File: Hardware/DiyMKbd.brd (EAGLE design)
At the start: 83 x 98 mm, 68 parts

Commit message: add gerber file
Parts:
- J1: value (none) -> 2.54 header
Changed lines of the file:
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@@
 <setting verticaltext="up"/>
 </settings>
-<grid distance="1" unitdist="mm" unit="mm" style="lines" multiple="1" display="yes" altdistance="0.025" altunitdist="inch" altunit="mm"/>
+<grid distance="0.5" unitdist="mm" unit="mm" style="lines" multiple="1" display="yes" altdistance="0.025" altunitdist="inch" altunit="mm"/>
 <layers>
 <layer number="1" name="Top" color="4" fill="1" visible="yes" active="yes"/>
@@
 <attribute name="VALUE" x="49.106" y="88.44" size="0.6096" layer="27" font="vector" ratio="20" rot="R270" align="top-center"/>
 </element>
-<element name="J1" library="SparkFun-Connectors" package="1X03_LOCK" value="" x="45.23" y="93.84" smashed="yes" rot="R270">
+<element name="J1" library="SparkFun-Connectors" package="1X03_LOCK" value="2.54 header" x="45.23" y="93.84" smashed="yes" rot="R270">
 <attribute name="NAME" x="47.627" y="95.11" size="1.016" layer="25" font="vector" rot="R270"/>
 <attribute name="VALUE" x="43.198" y="95.11" size="0.6096" layer="27" font="vector" ratio="20" rot="R270"/>
@@
 </element>
 <element name="D5" library="diode" package="SOD-123_MINI-SMA" value="CGRM4001-G" x="22.5" y="13" smashed="yes" rot="R270">
-<attribute name="NAME" x="23.643" y="16.048" size="1.016" layer="25" font="vector" rot="R270"/>
+<attribute name="NAME" x="22.143" y="10.048" size="1.016" layer="25" font="vector" rot="R270"/>
 <attribute name="VALUE" x="20.087" y="16.048" size="1.27" layer="27" rot="R270"/>
 </element>
 <element name="D1" library="diode" package="SOD-123_MINI-SMA" value="CGRM4001-G" x="41.5" y="13" smashed="yes" rot="R270">
-<attribute name="NAME" x="42.643" y="16.048" size="1.016" layer="25" font="vector" rot="R270"/>
+<attribute name="NAME" x="41.143" y="10.048" size="1.016" layer="25" font="vector" rot="R270"/>
 <attribute name="VALUE" x="39.087" y="16.048" size="1.27" layer="27" rot="R270"/>
 </element>
 <element name="D2" library="diode" package="SOD-123_MINI-SMA" value="CGRM4001-G" x="60.5" y="13" smashed="yes" rot="R270">
-<attribute name="NAME" x="61.643" y="16.048" size="1.016" layer="25" font="vector" rot="R270"/>
+<attribute name="NAME" x="60.143" y="10.048" size="1.016" layer="25" font="vector" rot="R270"/>
 <attribute name="VALUE" x="58.087" y="16.048" size="1.27" layer="27" rot="R270"/>
 </element>
 <element name="D3" library="diode" package="SOD-123_MINI-SMA" value="CGRM4001-G" x="79.5" y="13" smashed="yes" rot="R270">
-<attribute name="NAME" x="80.643" y="16.048" size="1.016" layer="25" font="vector" rot="R270"/>
+<attribute name="NAME" x="79.143" y="10.048" size="1.016" layer="25" font="vector" rot="R270"/>
 <attribute name="VALUE" x="77.087" y="16.048" size="1.27" layer="27" rot="R270"/>
 </element>
 <element name="D4" library="diode" package="SOD-123_MINI-SMA" value="CGRM4001-G" x="22.5" y="31" smashed="yes" rot="R270">
-<attribute name="NAME" x="23.643" y="34.048" size="1.016" layer="25" font="vector" rot="R270"/>
+<attribute name="NAME" x="22.143" y="28.048" size="1.016" layer="25" font="vector" rot="R270"/>
 <attribute name="VALUE" x="20.087" y="34.048" size="1.27" layer="27" rot="R270"/>
 </element>
 <element name="D6" library="diode" package="SOD-123_MINI-SMA" value="CGRM4001-G" x="41.5" y="31" smashed="yes" rot="R270">
-<attribute name="NAME" x="42.643" y="34.048" size="1.016" layer="25" font="vector" rot="R270"/>
+<attribute name="NAME" x="41.143" y="27.548" size="1.016" layer="25" font="vector" rot="R270"/>
 <attribute name="VALUE" x="39.087" y="34.048" size="1.27" layer="27" rot="R270"/>
 </element>
 <element name="D7" library="diode" package="SOD-123_MINI-SMA" value="CGRM4001-G" x="60.5" y="31" smashed="yes" rot="R270">
-<attribute name="NAME" x="61.643" y="34.048" size="1.016" layer="25" font="vector" rot="R270"/>
+<attribute name="NAME" x="60.143" y="27.548" size="1.016" layer="25" font="vector" rot="R270"/>
 <attribute name="VALUE" x="58.087" y="34.048" size="1.27" layer="27" rot="R270"/>
 </element>
 <element name="D8" library="diode" package="SOD-123_MINI-SMA" value="CGRM4001-G" x="79.5" y="31" smashed="yes" rot="R270">
-<attribute name="NAME" x="80.643" y="34.048" size="1.016" layer="25" font="vector" rot="R270"/>
+<attribute name="NAME" x="79.143" y="27.548" size="1.016" layer="25" font="vector" rot="R270"/>
 <attribute name="VALUE" x="77.087" y="34.048" size="1.27" layer="27" rot="R270"/>
 </element>
 <element name="D9" library="diode" package="SOD-123_MINI-SMA" value="CGRM4001-G" x="22.5" y="50" smashed="yes" rot="R270">
-<attribute name="NAME" x="23.643" y="53.048" size="1.016" layer="25" font="vector" rot="R270"/>
+<attribute name="NAME" x="22.143" y="47.048" size="1.016" layer="25" font="vector" rot="R270"/>
 <attribute name="VALUE" x="20.087" y="53.048" size="1.27" layer="27" rot="R270"/>
 </element>
 <element name="D10" library="diode" package="SOD-123_MINI-SMA" value="CGRM4001-G" x="41.5" y="50" smashed="yes" rot="R270">
-<attribute name="NAME" x="42.643" y="53.048" size="1.016" layer="25" font="vector" rot="R270"/>
+<attribute name="NAME" x="41.143" y="47.048" size="1.016" layer="25" font="vector" rot="R270"/>
 <attribute name="VALUE" x="39.087" y="53.048" size="1.27" layer="27" rot="R270"/>
 </element>
 <element name="D11" library="diode" package="SOD-123_MINI-SMA" value="CGRM4001-G" x="60.5" y="50" smashed="yes" rot="R270">
-<attribute name="NAME" x="61.643" y="53.048" size="1.016" layer="25" font="vector" rot="R270"/>
+<attribute name="NAME" x="60.143" y="47.048" size="1.016" layer="25" font="vector" rot="R270"/>
 <attribute name="VALUE" x="58.087" y="53.048" size="1.27" layer="27" rot="R270"/>
 </element>
 <element name="D12" library="diode" package="SOD-123_MINI-SMA" value="CGRM4001-G" x="79.5" y="50" smashed="yes" rot="R270">
-<attribute name="NAME" x="80.643" y="53.048" size="1.016" layer="25" font="vector" rot="R270"/>
+<attribute name="NAME" x="79.143" y="47.048" size="1.016" layer="25" font="vector" rot="R270"/>
 <attribute name="VALUE" x="77.087" y="53.048" size="1.27" layer="27" rot="R270"/>
 </element>
 <element name="D13" library="diode" package="SOD-123_MINI-SMA" value="CGRM4001-G" x="22.5" y="69" smashed="yes" rot="R270">
-<attribute name="NAME" x="23.643" y="72.048" size="1.016" layer="25" font="vector" rot="R270"/>
+<attribute name="NAME" x="22.043" y="65.748" size="1.016" layer="25" font="vector" rot="R270"/>
 <attribute name="VALUE" x="20.087" y="72.048" size="1.27" layer="27" rot="R270"/>
 </element>
 <element name="D14" library="diode" package="SOD-123_MINI-SMA" value="CGRM4001-G" x="41.5" y="69" smashed="yes" rot="R270">
-<attribute name="NAME" x="42.643" y="72.048" size="1.016" layer="25" font="vector" rot="R270"/>
+<attribute name="NAME" x="41.143" y="66.048" size="1.016" layer="25" font="vector" rot="R270"/>
 <attribute name="VALUE" x="39.087" y="72.048" size="1.27" layer="27" rot="R270"/>
 </element>
 <element name="D15" library="diode" package="SOD-123_MINI-SMA" value="CGRM4001-G" x="60.5" y="69" smashed="yes" rot="R270">
-<attribute name="NAME" x="61.643" y="72.048" size="1.016" layer="25" font="vector" rot="R270"/>
+<attribute name="NAME" x="60.143" y="66.048" size="1.016" layer="25" font="vector" rot="R270"/>
 <attribute name="VALUE" x="58.087" y="72.048" size="1.27" layer="27" rot="R270"/>
 </element>
 <element name="D16" library="diode" package="SOD-123_MINI-SMA" value="CGRM4001-G" x="79.5" y="69" smashed="yes" rot="R270">
-<attribute name="NAME" x="80.643" y="72.048" size="1.016" layer="25" font="vector" rot="R270"/>
+<attribute name="NAME" x="79.143" y="66.048" size="1.016" layer="25" font="vector" rot="R270"/>
 <attribute name="VALUE" x="77.087" y="72.048" size="1.27" layer="27" rot="R270"/>
 </element>

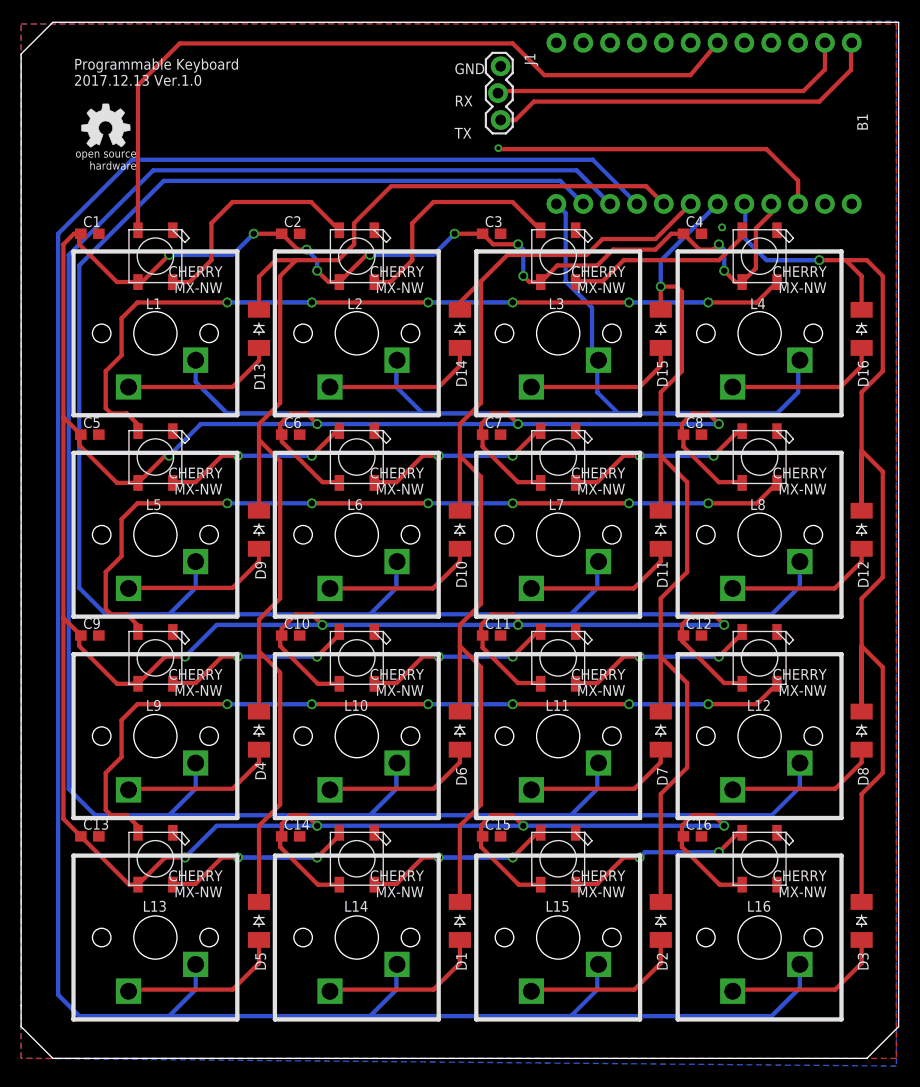
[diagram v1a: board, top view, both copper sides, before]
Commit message: Add hole & rounding edge
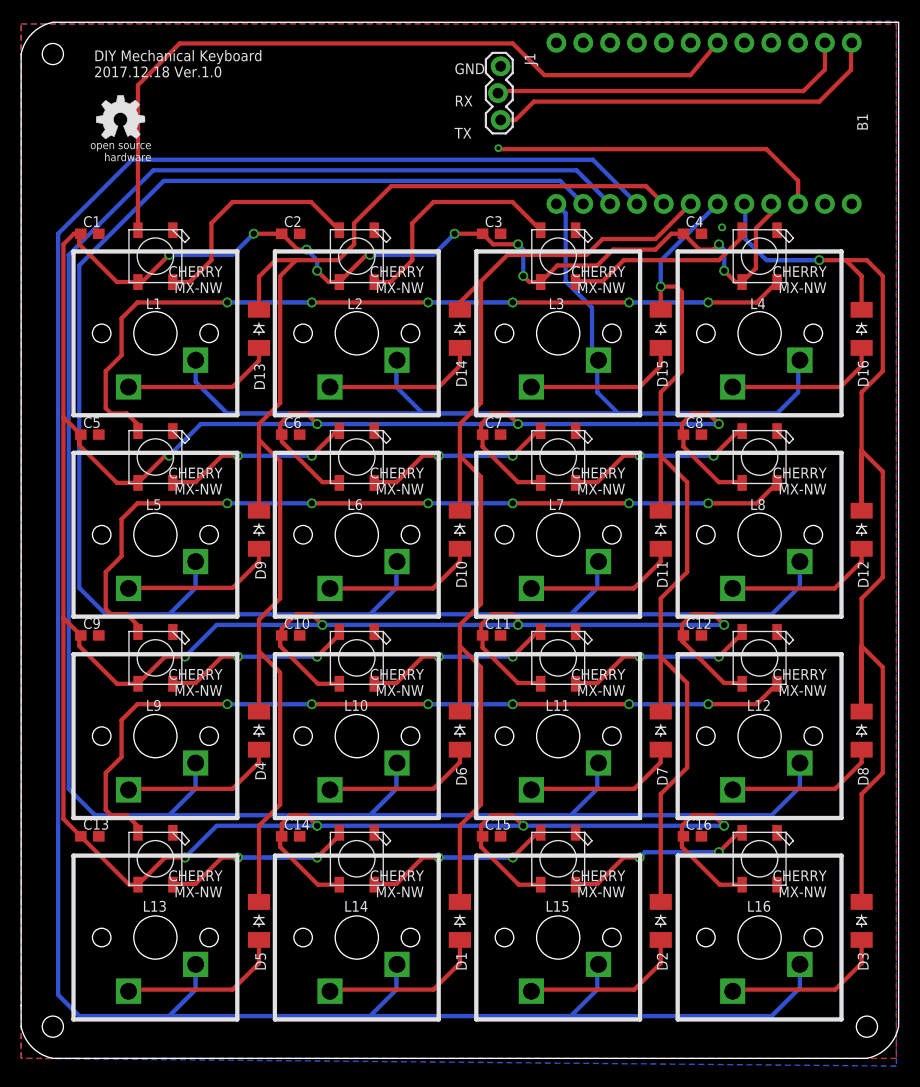
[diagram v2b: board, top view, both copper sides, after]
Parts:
- moved GOLD_ORB_SM1 1.61 mm to (9.40, 88.8)
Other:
- board text added: "DIY Mechanical Keyboard 2017.12.18 Ver.1.0"
- board text removed: "Programmable Keyboard 2017.12.13 Ver.1.0"
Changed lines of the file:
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@@
 <setting verticaltext="up"/>
 </settings>
-<grid distance="0.5" unitdist="mm" unit="mm" style="lines" multiple="1" display="yes" altdistance="0.025" altunitdist="inch" altunit="mm"/>
+<grid distance="0.1" unitdist="mm" unit="mm" style="lines" multiple="1" display="yes" altdistance="0.025" altunitdist="inch" altunit="mm"/>
 <layers>
 <layer number="1" name="Top" color="4" fill="1" visible="yes" active="yes"/>
@@
 <wire x1="0" y1="95" x2="0" y2="5" width="0" layer="20"/>
 <wire x1="0" y1="5" x2="0" y2="3" width="0" layer="20"/>
-<wire x1="3" y1="0" x2="0" y2="3" width="0" layer="20"/>
-<wire x1="83" y1="3" x2="80" y2="0" width="0" layer="20"/>
-<wire x1="3" y1="98" x2="0" y2="95" width="0" layer="20"/>
 <text x="41" y="87" size="1.016" layer="25" font="vector">GND
 RX
 TX</text>
-<text x="5" y="92" size="1.016" layer="25">Programmable Keyboard
-2017.12.13 Ver.1.0</text>
+<text x="6.9" y="92.8" size="1.016" layer="25">DIY Mechanical Keyboard
+2017.12.18 Ver.1.0</text>
+<wire x1="3" y1="0" x2="0" y2="3" width="0" layer="20" curve="-67.380135"/>
+<wire x1="0" y1="95" x2="3" y2="98" width="0" layer="20" curve="-67.380135"/>
+<wire x1="83" y1="3" x2="80" y2="0" width="0" layer="20" curve="-67.380135"/>
+<hole x="3" y="3" drill="2"/>
+<hole x="80" y="3" drill="2"/>
+<hole x="3" y="95" drill="2"/>
 </plain>
 <attributes>
@@
 <attribute name="VALUE" x="77.087" y="72.048" size="1.27" layer="27" rot="R270"/>
 </element>
-<element name="GOLD_ORB_SM1" library="oshw" package="OSHW_5MM" value="OSHWLOGOLOGO5MM" x="8" y="88" smashed="yes"/>
+<element name="GOLD_ORB_SM1" library="oshw" package="OSHW_5MM" value="OSHWLOGOLOGO5MM" x="9.4" y="88.8" smashed="yes"/>
 </elements>
 <signals>
